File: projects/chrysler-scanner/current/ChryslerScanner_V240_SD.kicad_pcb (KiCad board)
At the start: 4 copper layers, 110 x 55 mm, 263 parts, among them J1 226A-1202, J2 USB-C, J3 I2C, J4 microSD / DM3AT-SF-PEJM5, Q1 CJ3439KDW, Q10 HSW4602, Q11 HSW4602, Q12 HSW4602, Q13 HSW4602, Q14 HSW4602, Q15 HSW4602, Q16 CJ3439KDW, Q17 AO3400, Q18 AO3400, Q19 AO3400, Q2 2N7002DW, Q20 AO3400, Q3 2N7002DW, Q4 2N7002DW, Q5 UMH3N, Q6 CJ3439KDW, Q7 HSSK8811, Q8 HSW4602, Q9 HSW4602, SW1 RESET, SW2 BOOT, SW3 LOG / SAFE STOP, U1 SY6283, U10 ESP32-PICO-V3-02, U11 USBLC6-2SC6, U12 CP2102, U13 74LVC2G66, U14 74LVC2G66, U15 74LVC2G66, U16 TS391C, U17 74LVC1G17, U18 74LVC1G14, U19 AW9523B, U2 LMR14010, U20 MCP1825S-3302E/DB, U3 TLV76750DRV, U4 TLV76733DRV, U5 LGS6302, U6 LMR14010, U7 LMR14010, U8 TLV76701DRV, U9 TS391C

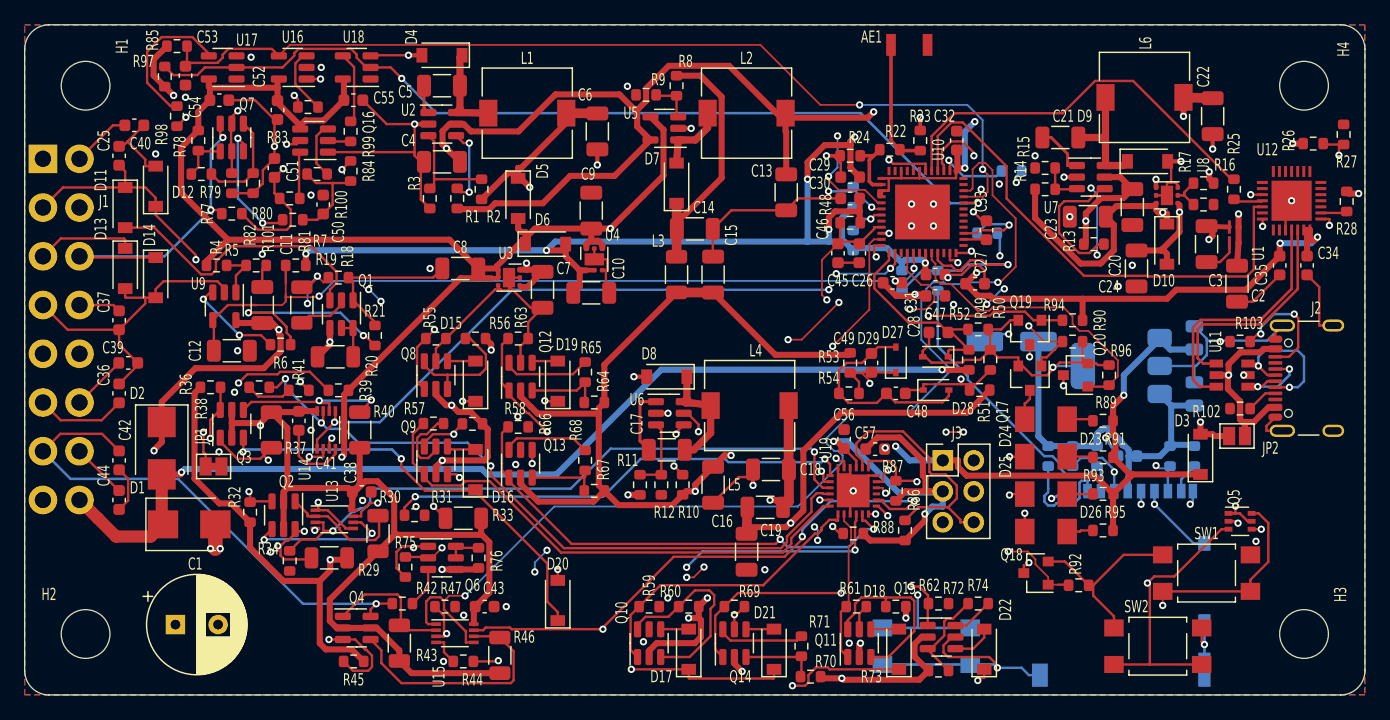
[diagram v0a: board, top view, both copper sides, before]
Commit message: Finish scanner routing and add hierarchical system schematics
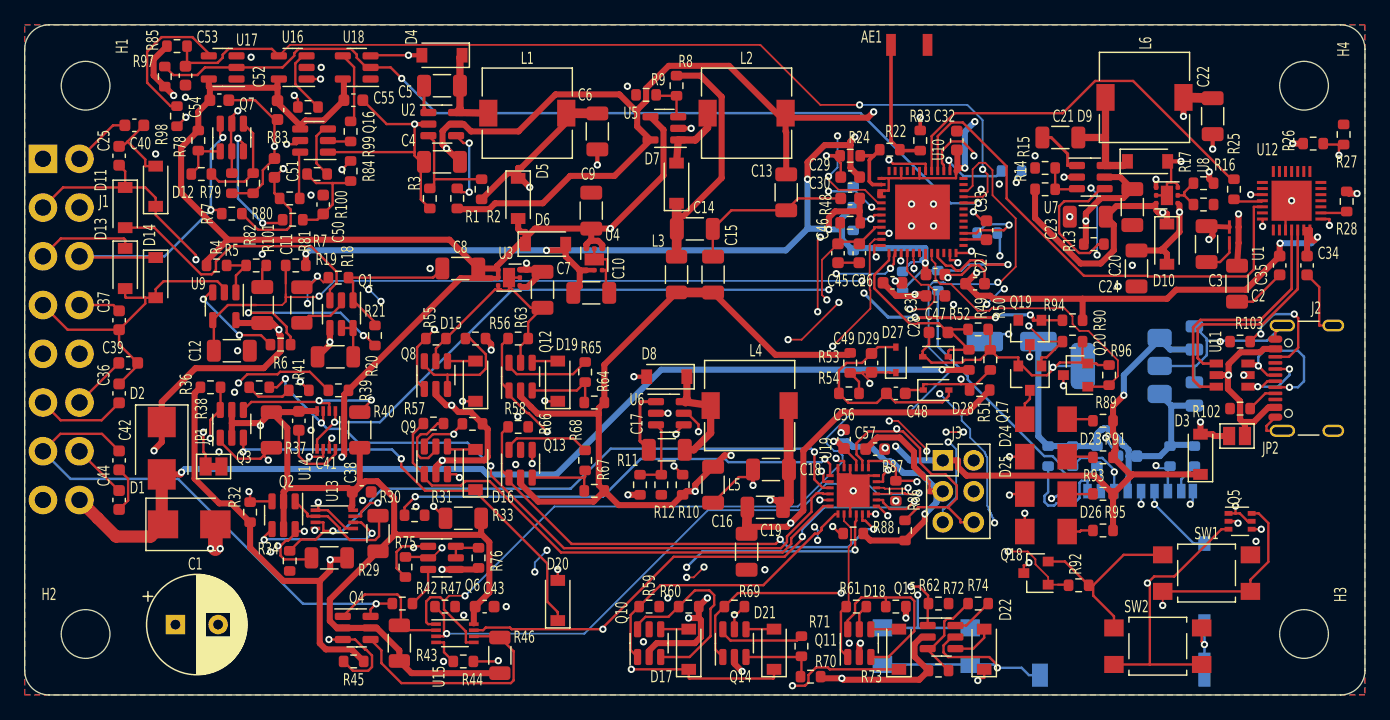
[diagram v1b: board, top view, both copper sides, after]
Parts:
- moved R112 0.09 mm to (172.1, 121.1)
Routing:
- net RX15_EN: track 3.70 -> 51.6 mm, vias 1 -> 2
- net TX_LED: track 6.72 -> 34.9 mm, vias 1 -> 4
- net SDA: track 67.0 -> 53.3 mm, vias 1 -> 4
- net SCL: track 53.6 -> 59.5 mm, vias 2 -> 3
- net LOG_BUTTON: track 52.9 -> 58.0 mm, vias 3 -> 5
- net PCI_RX: track 63.9 -> 67.4 mm, vias 2 -> 3
- net RX7_BIAS_EN: track 48.8 -> 52.3 mm
- net GND: track 332.8 -> 330.0 mm, vias 69 -> 70
- net PWR_LED: track 21.6 -> 23.2 mm, vias 2 -> 5
- net VPP: track 111.0 -> 109.5 mm
- net N_C5_2: track 8.88 -> 7.58 mm
- net VBB: track 113.7 -> 112.6 mm
- net N_C17_2: track 10.5 -> 9.57 mm
- net +3.3V: track 348.4 -> 347.7 mm, vias 17 -> 18
- net RX2: track 90.9 -> 90.3 mm
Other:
- board text added: "ROUTED - PROTOTYPE HARDWARE / FIRMWARE DEFERRED"
- board text added: "SD LOGGER - ROUTED / FIRMWARE DEFERRED"
- board text removed: "SD LOGGER - NEW CIRCUIT UNROUTED / FIRMWARE DEFERRED"
- board text removed: "UNROUTED - ENGINEERING REVIEW REQUIRED"

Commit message: Fix scanner protection, ADC isolation and health watchdog
Coordinate the bounded 12 V input clamp and programming FET/capacitor ratings, add powered-off ADC isolation, and supervise the AW9523B permit with a dedicated GPIO13 health heartbeat. Preserve original placements and document all deliberate source-PDF deviations.

Validation: native ERC and full DRC/parity/refill report zero findings; strict preservation/connectivity audit and final adversarial review pass within the documented prototype bounds. Regenerate Rev C PDF, BOM, manufacturing exports, processing sites and verified portable archives. Compatible firmware and bench/mechanical qualification remain required.
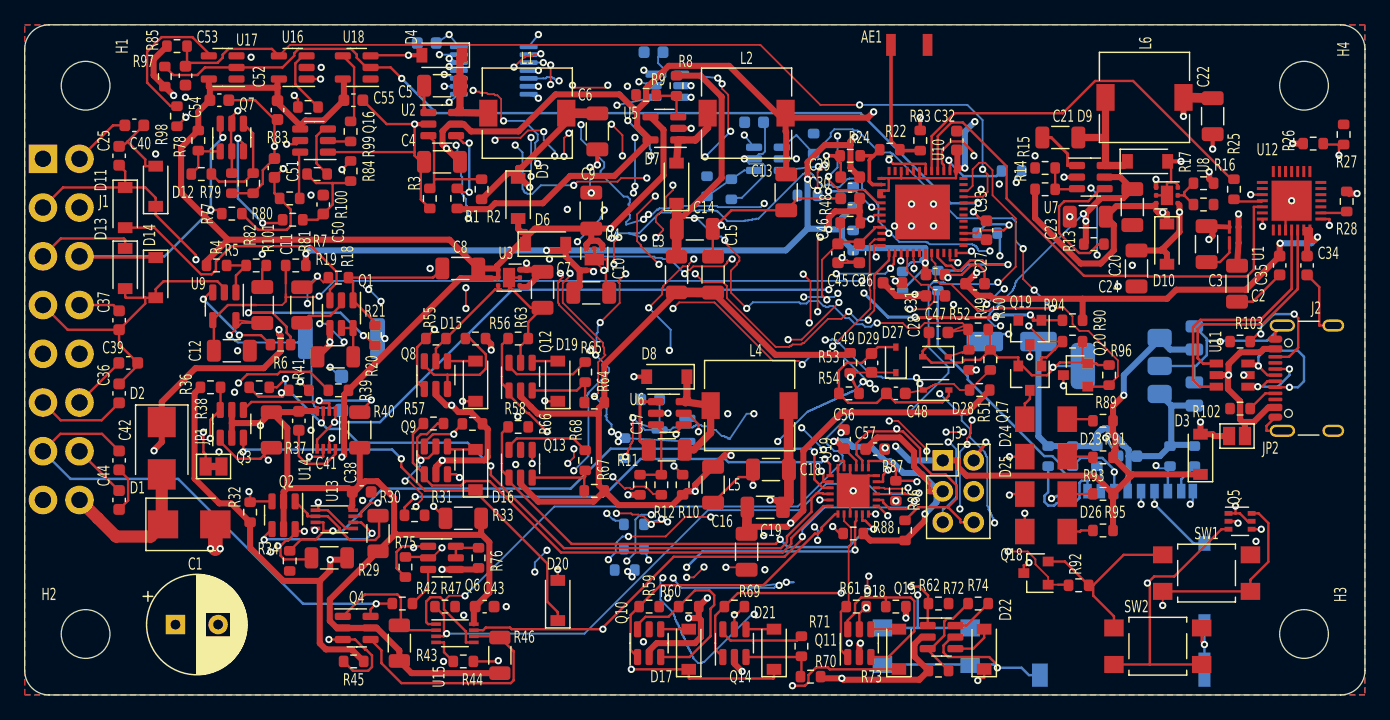
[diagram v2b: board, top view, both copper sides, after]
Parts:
- added C62: 100nF 16V X7R, Capacitor_SMD:C_0603_1608Metric, B.Cu at (133.0, 101.5)
- added C63: 100nF 16V X7R, Capacitor_SMD:C_0603_1608Metric, B.Cu at (159.9, 108.0)
- added C64: 100nF 16V X7R, Capacitor_SMD:C_0603_1608Metric, B.Cu at (151.6, 102.2)
- added C65: 100nF 16V X7R, Capacitor_SMD:C_0603_1608Metric, B.Cu at (151.3, 130.8)
- added D30: BZT52H-B15, Diode_SMD:D_SOD-123F, B.Cu at (126.0, 130.2)
- added R115: 100k 0.1% 25ppm, Resistor_SMD:R_0603_1608Metric, B.Cu at (164.2, 114.0)
- added R116: 191k 1%, Resistor_SMD:R_0603_1608Metric, B.Cu at (158.0, 113.5)
- added R117: 100k 1%, Resistor_SMD:R_0603_1608Metric, B.Cu at (156.0, 113.2)
- added R118: 10k 1%, Resistor_SMD:R_0603_1608Metric, B.Cu at (164.8, 109.8)
- added R119: 10k 1%, Resistor_SMD:R_0603_1608Metric, B.Cu at (149.2, 134.8)
- added R120: 100k 1%, Resistor_SMD:R_0603_1608Metric, B.Cu at (150.0, 141.0)
- added R121: 100k 1%, Resistor_SMD:R_0603_1608Metric, B.Cu at (150.0, 143.0)
- added R122: 100k 1%, Resistor_SMD:R_0603_1608Metric, B.Cu at (149.2, 144.8)
- added R123: 1k 1W 1%, Resistor_SMD:R_2512_6332Metric, B.Cu at (126.0, 125.8)
- added U21: TMUX1511PWR, Package_SO:TSSOP-14_4.4x5mm_P0.65mm, B.Cu at (138.5, 103.8)
- added U22: LTC6993HS6-2#TRMPBF, Package_TO_SOT_SMD:TSOT-23-6, B.Cu at (161.0, 111.0)
- added U23: SN74LVC1G11DBVR, Package_TO_SOT_SMD:SOT-23-6, B.Cu at (152.8, 105.0)
- added U24: TLV803EA30DBZR, Package_TO_SOT_SMD:SOT-23-3, B.Cu at (153.2, 133.2)
- D1: value SMBJ30CA -> SMBJ16CA
- Q10, Q11, Q8, Q9: value HSW4602 -> DMC3071LVT-7
- Q12, Q13, Q14, Q15: value HSW4602 -> DMG6601LVT-7
- R49, R51: value 8.66kΩ -> 22k 1%
- R50, R52, R54: value 1.62kΩ -> 1.62k 1%
- R53: value 18.2kΩ -> 22k 1%
- R64, R67, R70, R73: value 4.7kΩ -> 4.7k 1%
- R65, R68, R71, R74: value 1.1kΩ -> 8.2k 1%
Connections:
- C11 pad 2: +12V -> PCI_VCC
- C47 pad 1: V_BA -> V_BA_PRE
- C48 pad 1: V_BT -> V_BT_PRE
- C49 pad 1: V_PR -> V_PR_PRE
- D27 pad 1: V_BA -> V_BA_PRE
- D28 pad 1: V_BT -> V_BT_PRE
- D29 pad 1: V_PR -> V_PR_PRE
- R49 pad 1: J1962-16 -> +12V
- R49 pad 2: V_BA -> V_BA_PRE
- R50 pad 1: V_BA -> V_BA_PRE
- R51 pad 2: V_BT -> V_BT_PRE
- R52 pad 1: V_BT -> V_BT_PRE
- R53 pad 2: V_PR -> V_PR_PRE
- R54 pad 1: V_PR -> V_PR_PRE
- U9 pad 5: +12V -> PCI_VCC
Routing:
- net V_BT: track 30.9 -> 158.0 mm, vias 4 -> 17
- net +3.3V: track 347.7 -> 449.1 mm, vias 18 -> 32
- net LOGIC_PG: track 0.00 -> 99.9 mm, vias 0 -> 17
- net V_PR: track 22.0 -> 120.2 mm, vias 2 -> 17
- net V_BA: track 17.3 -> 94.2 mm, vias 0 -> 20
- net GND: track 330.0 -> 402.4 mm, vias 70 -> 98
- net J1962-16: track 82.9 -> 12.6 mm, vias 2 -> 0
- net V_BA_PRE: track 0.00 -> 68.2 mm, vias 0 -> 9
- net N_R88_2: track 8.10 -> 75.4 mm, vias 2 -> 14
- net V_BT_PRE: track 0.00 -> 61.3 mm, vias 0 -> 10
- net V_PR_PRE: track 0.00 -> 60.3 mm, vias 0 -> 8
- net ACT_LED: track 24.7 -> 63.6 mm, vias 0 -> 3
- net EN: track 70.2 -> 101.8 mm, vias 4 -> 10
- net +12V: track 159.8 -> 186.5 mm, vias 5 -> 11
- net PCI_VCC: track 0.00 -> 20.1 mm, vias 0 -> 1
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
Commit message: Move C61 to top side near microSD supply and verify routing
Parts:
- C61: moved to F.Cu
- moved C61 12.0 mm to (193.0, 127.0), turned to 90 degrees
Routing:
- net SD_3V3: track 33.3 -> 27.5 mm, vias 0 -> 1
- net GND: track 402.4 -> 403.9 mm, vias 98 -> 99
